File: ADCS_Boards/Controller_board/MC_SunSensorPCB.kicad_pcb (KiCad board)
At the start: 4 copper layers, 90.2 x 95.9 mm, 5 parts, among them J1 PC104_Connector

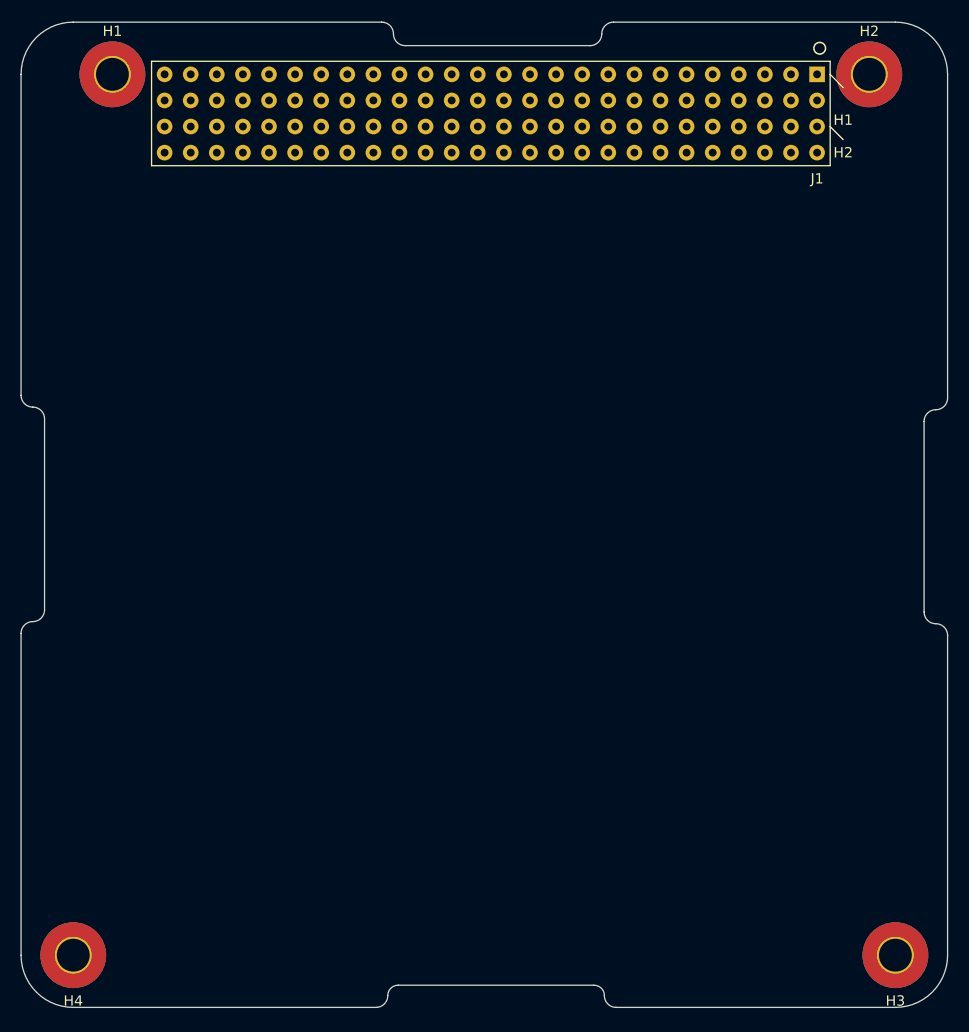
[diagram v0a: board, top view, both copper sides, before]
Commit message: adcs: Updated ADCS Controller board with latest status from Yasin
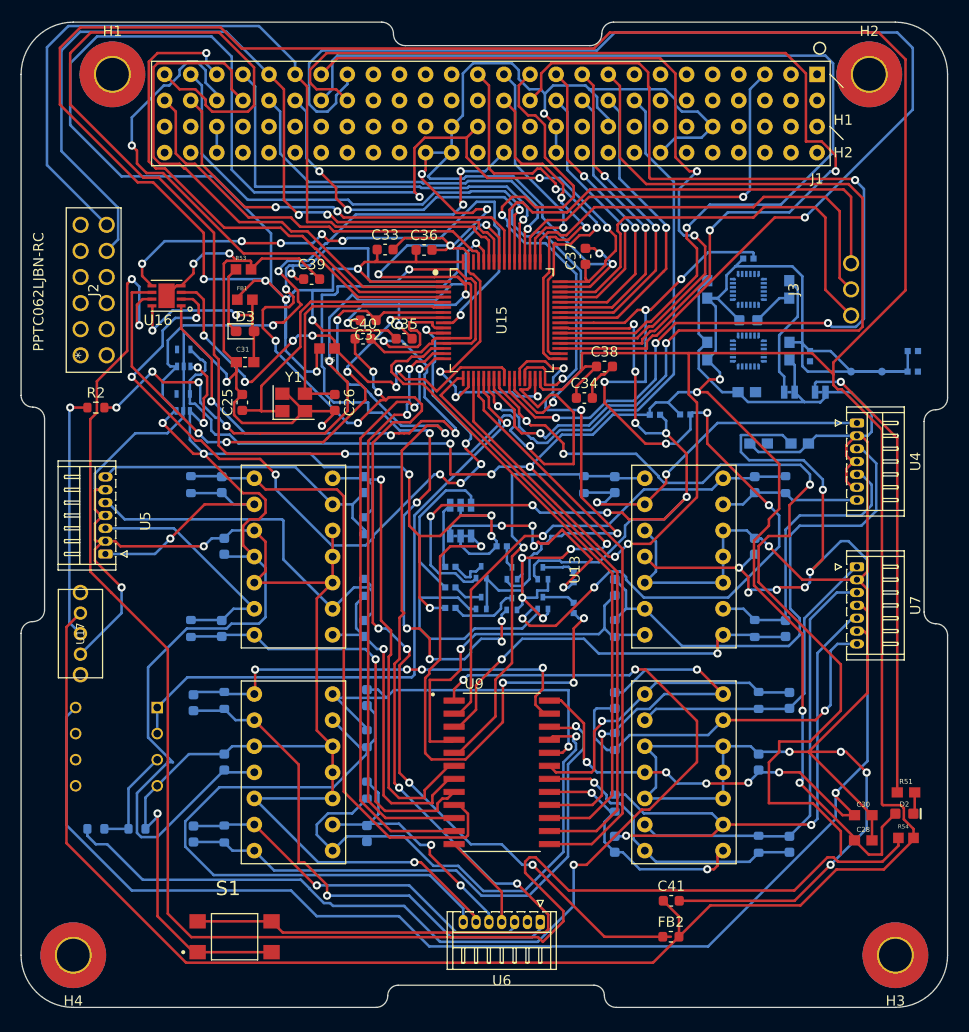
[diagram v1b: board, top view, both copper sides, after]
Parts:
- added C1: 1.0uF, SparkFun_IMU_Breakout_ICM-20948:0603, B.Cu at (184.0, 79.0)
- added C10: C, Capacitor_SMD:C_0603_1608Metric, B.Cu at (184.0, 113.0)
- added C11: C, Capacitor_SMD:C_0603_1608Metric, B.Cu at (184.0, 127.0)
- added C12: C, Capacitor_SMD:C_0603_1608Metric, B.Cu at (126.0, 113.2)
- added C13: C, Capacitor_SMD:C_0603_1608Metric, B.Cu at (126.0, 126.0)
- added C14: C, Capacitor_SMD:C_0603_1608Metric, B.Cu at (167.0, 92.0)
- added C15: C, Capacitor_SMD:C_0603_1608Metric, B.Cu at (167.0, 102.0)
- added C16: C, Capacitor_SMD:C_0603_1608Metric, B.Cu at (167.0, 127.0)
- added C17: C, Capacitor_SMD:C_0603_1608Metric, B.Cu at (167.0, 113.0)
- added C18: C, Capacitor_SMD:C_0603_1608Metric, B.Cu at (142.9, 126.0)
- added C19: C, Capacitor_SMD:C_0603_1608Metric, B.Cu at (142.9, 112.7)
- added C2: C, Capacitor_SMD:C_0603_1608Metric, B.Cu at (129.0, 119.0)
- added C20: C, Capacitor_SMD:C_0603_1608Metric, B.Cu at (183.6, 106.0)
- added C21: C, Capacitor_SMD:C_0603_1608Metric, B.Cu at (180.6, 92.0)
- added C22: 0.1uF, SparkFun_IMU_Breakout_ICM-20948:0603, B.Cu at (176.0, 79.0)
- added C23: 0.1uF, SparkFun_IMU_Breakout_ICM-20948:0603, B.Cu at (179.8, 83.0)
- added C24: 1.0uF, SparkFun_IMU_Breakout_ICM-20948:0603, B.Cu at (185.0, 88.0)
- added C25: 10p, Capacitor_SMD:C_0603_1608Metric, F.Cu at (130.8, 84.0)
- added C26: 10p, Capacitor_SMD:C_0603_1608Metric, F.Cu at (139.8, 84.0)
- added C27: 1.0uF, SparkFun_IMU_Breakout_ICM-20948:0603, B.Cu at (176.0, 73.0)
- added C28: 0.1uF, SparkFun_IMU_Breakout_ICM-20948:0603, F.Cu at (191.2, 126.6)
- added C29: 0.1uF, SparkFun_IMU_Breakout_ICM-20948:0603, B.Cu at (181.0, 88.0)
- added C3: C, Capacitor_SMD:C_0603_1608Metric, B.Cu at (128.8, 92.0)
- added C30: 1.0uF, SparkFun_IMU_Breakout_ICM-20948:0603, F.Cu at (191.2, 124.2)
- added C31: 100n, STM32_Breakout:CAPC1608X90, F.Cu at (131.0, 80.1)
- added C32: 100n, Capacitor_SMD:C_0603_1608Metric, F.Cu at (143.0, 76.0)
- added C33: 10u, Capacitor_SMD:C_0603_1608Metric, F.Cu at (144.7, 69.1)
- added C34: 100n, Capacitor_SMD:C_0603_1608Metric, F.Cu at (164.0, 83.6)
- added C35: 100n, Capacitor_SMD:C_0603_1608Metric, F.Cu at (146.5, 77.8)
- added C36: 100n, Capacitor_SMD:C_0603_1608Metric, F.Cu at (148.4, 69.2)
- added C37: 100n, Capacitor_SMD:C_0603_1608Metric, F.Cu at (164.2, 69.8)
- added C38: 100n, Capacitor_SMD:C_0603_1608Metric, F.Cu at (166.0, 80.5)
- added C39: 10n, Capacitor_SMD:C_0603_1608Metric, F.Cu at (137.5, 72.0)
- added C4: C, Capacitor_SMD:C_0603_1608Metric, B.Cu at (128.8, 106.0)
- added C40: 1u, Capacitor_SMD:C_0603_1608Metric, F.Cu at (142.5, 77.8)
- added C41: 1u, Capacitor_SMD:C_0603_1608Metric, F.Cu at (172.5, 132.5)
- added C5: C, Capacitor_SMD:C_0603_1608Metric, B.Cu at (142.6, 106.0)
- added C6: C, Capacitor_SMD:C_0603_1608Metric, B.Cu at (142.6, 92.0)
- added C7: C, Capacitor_SMD:C_0603_1608Metric, B.Cu at (129.0, 98.0)
- added C8: C, Capacitor_SMD:C_0603_1608Metric, B.Cu at (180.6, 98.0)
- added C9: C, Capacitor_SMD:C_0603_1608Metric, B.Cu at (181.0, 119.0)
- added D1: RED, SparkFun_IMU_Breakout_ICM-20948:LED-0603, B.Cu at (180.0, 76.0)
- added D2: RED, SparkFun_IMU_Breakout_ICM-20948:LED-0603, F.Cu at (195.2, 124.0)
- added D3: RED, LED_SMD:LED_0603_1608Metric_Pad1.05x0.95mm_HandSolder, F.Cu at (131.0, 77.1)
- added FB1: 100R @ 100 MHz, STM32_Breakout:INDUC1607X60N, F.Cu at (131.0, 74.0)
- added FB2: FerriteBead, Inductor_SMD:L_0603_1608Metric, F.Cu at (172.5, 136.0)
- added J2: PPTC062LJBN-RC, Footprints_QSAT:PPTC062LJBN-RC, F.Cu at (115.0, 79.4)
- added J3: Conn_01x03_Female, Footprints_QSAT:1x3_Connector_Female, F.Cu at (184.9, 73.0)
- added JP2: I2C PU, SparkFun_IMU_Breakout_ICM-20948:SMT-JUMPER_3_2-NC_TRACE_SILK, B.Cu at (152.0, 94.0)
- added JP3: LED, SparkFun_IMU_Breakout_ICM-20948:SMT-JUMPER_2_NC_TRACE_SILK, B.Cu at (184.0, 83.0)
- added JP5: I2C PU, SparkFun_IMU_Breakout_ICM-20948:SMT-JUMPER_3_2-NC_TRACE_SILK, B.Cu at (152.0, 97.0)
- added JP6: LED, SparkFun_IMU_Breakout_ICM-20948:SMT-JUMPER_2_NC_TRACE_SILK, B.Cu at (187.0, 83.0)
- added Q12: 20V/0.2A/8MHz/1.2Ω/1Vth, SparkFun_IMU_Breakout_ICM-20948:SOT-416FL, B.Cu at (160.0, 100.1)
- added Q14: 20V/0.2A/8MHz/1.2Ω/1Vth, SparkFun_IMU_Breakout_ICM-20948:SOT-416FL, B.Cu at (157.0, 103.1)
- added Q3: 20V/0.2A/8MHz/1.2Ω/1Vth, SparkFun_IMU_Breakout_ICM-20948:SOT-416FL, B.Cu at (154.0, 103.0)
- added Q4: 20V/0.2A/8MHz/1.2Ω/1Vth, SparkFun_IMU_Breakout_ICM-20948:SOT-416FL, B.Cu at (154.0, 100.0)
- added Q6: 20V/0.2A/8MHz/1.2Ω/1Vth, SparkFun_IMU_Breakout_ICM-20948:SOT-416FL, B.Cu at (157.0, 100.1)
- added Q9: 20V/0.2A/8MHz/1.2Ω/1Vth, SparkFun_IMU_Breakout_ICM-20948:SOT-416FL, B.Cu at (160.0, 103.0)
- added R1: 2.2k, SparkFun_IMU_Breakout_ICM-20948:0402-TIGHT, B.Cu at (180.0, 70.0)
- added R10: R, Resistor_SMD:R_0603_1608Metric, B.Cu at (125.8, 106.0)
- added R11: R, Resistor_SMD:R_0603_1608Metric, B.Cu at (142.6, 102.0)
- added R12: R, Resistor_SMD:R_0603_1608Metric, B.Cu at (142.6, 96.0)
- added R13: R, Resistor_SMD:R_0603_1608Metric, B.Cu at (181.0, 113.0)
- added R14: R, Resistor_SMD:R_0603_1608Metric, B.Cu at (181.0, 127.0)
- added R15: R, Resistor_SMD:R_0603_1608Metric, B.Cu at (129.0, 113.0)
- added R16: R, Resistor_SMD:R_0603_1608Metric, B.Cu at (129.0, 126.0)
- added R17: R, Resistor_SMD:R_0603_1608Metric, B.Cu at (164.0, 92.0)
- added R18: R, Resistor_SMD:R_0603_1608Metric, B.Cu at (167.0, 106.0)
- added R19: R, Resistor_SMD:R_0603_1608Metric, B.Cu at (167.0, 123.0)
- added R2: 10k, Resistor_SMD:R_0603_1608Metric, F.Cu at (116.5, 84.5)
- added R20: R, Resistor_SMD:R_0603_1608Metric, B.Cu at (167.0, 117.0)
- added R21: R, Resistor_SMD:R_0603_1608Metric, B.Cu at (142.9, 121.7)
- added R22: R, Resistor_SMD:R_0603_1608Metric, B.Cu at (142.9, 116.7)
- added R23: R, Resistor_SMD:R_0603_1608Metric, B.Cu at (180.6, 106.0)
- added R24: R, Resistor_SMD:R_0603_1608Metric, B.Cu at (183.6, 92.0)
- added R26: 2.2k, SparkFun_IMU_Breakout_ICM-20948:0402-TIGHT, B.Cu at (173.9, 85.2)
- added R27: 2.2k, SparkFun_IMU_Breakout_ICM-20948:0402-TIGHT, B.Cu at (151.0, 102.0)
- added R28: 2.2k, SparkFun_IMU_Breakout_ICM-20948:0402-TIGHT, B.Cu at (196.0, 81.0)
- added R29: 2.2k, SparkFun_IMU_Breakout_ICM-20948:0402-TIGHT, B.Cu at (151.0, 100.0)
- added R3: 2.2k, SparkFun_IMU_Breakout_ICM-20948:0402-TIGHT, B.Cu at (163.0, 104.0)
- added R32: 2.2k, SparkFun_IMU_Breakout_ICM-20948:0402-TIGHT, B.Cu at (196.0, 79.0)
- added R33: 2.2k, SparkFun_IMU_Breakout_ICM-20948:0402-TIGHT, B.Cu at (156.0, 98.0)
- added R36: 220, SparkFun_IMU_Breakout_ICM-20948:0603, B.Cu at (184.0, 73.0)
- added R40: 2.2k, SparkFun_IMU_Breakout_ICM-20948:0402-TIGHT, B.Cu at (170.9, 85.2)
- added R43: 2.2k, SparkFun_IMU_Breakout_ICM-20948:0402-TIGHT, B.Cu at (163.0, 101.0)
- added R46: 2.2k, SparkFun_IMU_Breakout_ICM-20948:0402-TIGHT, B.Cu at (186.0, 79.5)
- added R47: 2.2k, SparkFun_IMU_Breakout_ICM-20948:0402-TIGHT, B.Cu at (151.0, 104.0)
- added R51: 220, SparkFun_IMU_Breakout_ICM-20948:0603, F.Cu at (195.3, 122.0)
- added R53: 2k2, STM32_Breakout:RESC1607X60N, F.Cu at (130.9, 71.0)
- added R54: 10k, STM32_Breakout:RESC1607X60N, F.Cu at (195.3, 126.4)
- added R55: 10k, STM32_Breakout:RESC1607X60N, F.Cu at (139.0, 78.8)
- added R7: 1Meg, Resistor_SMD:R_0603_1608Metric, B.Cu at (116.5, 125.5)
- added R8: 2Meg, Resistor_SMD:R_0603_1608Metric, B.Cu at (120.5, 125.5)
- added R9: R, Resistor_SMD:R_0603_1608Metric, B.Cu at (125.8, 92.0)
- added S1: TL3305CF260QG, Footprints_QSAT:SW_TL3305CF260QG, F.Cu at (130.0, 136.0)
- added TP1: 1.8V, SparkFun_IMU_Breakout_ICM-20948:PAD.03X.03, B.Cu at (193.0, 81.0)
- added TP2: 1.8V, SparkFun_IMU_Breakout_ICM-20948:PAD.03X.03, B.Cu at (190.0, 81.0)
- added U1: 9DoF IMU, SparkFun_IMU_Breakout_ICM-20948:QFN24-3X3, B.Cu at (180.0, 73.0)
- added U10: Op-Amp, Footprints_QSAT:Op-Amp, B.Cu at (129.4, 100.3)
- added U11: Op-Amp, Footprints_QSAT:Op-Amp, B.Cu at (167.4, 121.3)
- added U12: Op-Amp, Footprints_QSAT:Op-Amp, B.Cu at (129.4, 121.3)
- added U13: Op-Amp, Footprints_QSAT:Op-Amp, B.Cu at (167.4, 100.3)
- added U14: 1.8V/100mA, SparkFun_IMU_Breakout_ICM-20948:SC70, B.Cu at (125.0, 84.0)
- added U15: STM32F103RET6, Footprints_QSAT:QFP50P1200X1200X160-64N, F.Cu at (156.0, 76.0)
- added U16: MR25H10MDF, STM32_Breakout:SON65P300X300X95-8N, F.Cu at (123.4, 73.6)
- added U17: 1825232-1, Footprints_QSAT:1825232-1, F.Cu at (115.0, 106.5)
- added U2: 1.8V/100mA, SparkFun_IMU_Breakout_ICM-20948:SC70, B.Cu at (125.0, 79.7)
- added U3: 9DoF IMU, SparkFun_IMU_Breakout_ICM-20948:QFN24-3X3, B.Cu at (180.0, 79.0)
- added U4: DF13-7P-1.25DS(20), Connector_Hirose:Hirose_DF13-07P-1.25DS_1x07_P1.25mm_Horizontal, F.Cu at (190.6, 86.0)
- added U5: DF13-7P-1.25DS(20), Connector_Hirose:Hirose_DF13-07P-1.25DS_1x07_P1.25mm_Horizontal, F.Cu at (117.4, 98.8)
- added U6: DF13-7P-1.25DS(20), Connector_Hirose:Hirose_DF13-07P-1.25DS_1x07_P1.25mm_Horizontal, F.Cu at (159.8, 134.6)
- added U7: DF13-7P-1.25DS(20), Connector_Hirose:Hirose_DF13-07P-1.25DS_1x07_P1.25mm_Horizontal, F.Cu at (190.6, 100.0)
- added U8: LM358, Footprints_QSAT:DIP794W45P254L959H508Q8, B.Cu at (118.5, 117.5)
- added U9: CD74HC4067M96, Footprints_QSAT:SOIC127P1030X265-24N, F.Cu at (156.0, 120.0)
- added Y1: Crystal_GND24, Crystal:Crystal_SMD_3225-4Pin_3.2x2.5mm, F.Cu at (135.8, 84.0)
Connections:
- J1 pad 100: unconnected-(J1-Pad100) -> GND
- J1 pad 16: unconnected-(J1-Pad16) -> PA6
- J1 pad 17: unconnected-(J1-Pad17) -> PA7
- J1 pad 18: unconnected-(J1-Pad18) -> PA8
- J1 pad 19: unconnected-(J1-Pad19) -> PA9
- J1 pad 20: unconnected-(J1-Pad20) -> PA10
- J1 pad 21: unconnected-(J1-Pad21) -> PA11
- J1 pad 22: unconnected-(J1-Pad22) -> PA12
- J1 pad 23: unconnected-(J1-Pad23) -> PB10
- J1 pad 24: unconnected-(J1-Pad24) -> PB0
- J1 pad 25: unconnected-(J1-Pad25) -> PA15
- J1 pad 26: unconnected-(J1-Pad26) -> PB12
- J1 pad 27: unconnected-(J1-Pad27) -> PB13
- J1 pad 37: unconnected-(J1-Pad37) -> PB14
- J1 pad 38: unconnected-(J1-Pad38) -> PB15
- J1 pad 39: unconnected-(J1-Pad39) -> PC6
- J1 pad 40: unconnected-(J1-Pad40) -> PC7
- J1 pad 41: unconnected-(J1-Pad41) -> Net-(J1-Pad41)
- J1 pad 42: unconnected-(J1-Pad42) -> PB1
- J1 pad 43: unconnected-(J1-Pad43) -> Net-(J1-Pad43)
- J1 pad 44: unconnected-(J1-Pad44) -> PC11
- J1 pad 45: unconnected-(J1-Pad45) -> PC12
- J1 pad 46: unconnected-(J1-Pad46) -> PC13
- J1 pad 47: unconnected-(J1-Pad47) -> PC14
- J1 pad 48: unconnected-(J1-Pad48) -> PC15
- J1 pad 49: unconnected-(J1-Pad49) -> PD2
- J1 pad 5: unconnected-(J1-Pad5) -> PC10
- J1 pad 50: unconnected-(J1-Pad50) -> PB4
- J1 pad 51: unconnected-(J1-Pad51) -> PB11
- J1 pad 52: unconnected-(J1-Pad52) -> PB8
- J1 pad 61: unconnected-(J1-Pad61) -> GND
- J1 pad 66: unconnected-(J1-Pad66) -> GND
- J1 pad 69: unconnected-(J1-Pad69) -> GND
- J1 pad 73: unconnected-(J1-Pad73) -> GND
- J1 pad 74: unconnected-(J1-Pad74) -> GND
- J1 pad 78: unconnected-(J1-Pad78) -> +5V
- J1 pad 79: unconnected-(J1-Pad79) -> +3V3
- J1 pad 81: unconnected-(J1-Pad81) -> GND
- J1 pad 82: unconnected-(J1-Pad82) -> GND
- J1 pad 84: unconnected-(J1-Pad84) -> GND
- J1 pad 99: unconnected-(J1-Pad99) -> GND
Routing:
- net GND: track 0.00 -> 668.1 mm, vias 0 -> 26
- net +3V3: track 0.00 -> 603.4 mm, vias 0 -> 11
- net +5V: track 0.00 -> 423.0 mm, vias 0 -> 24
- net GPIO1: track 0.00 -> 254.8 mm, vias 0 -> 5
- net 1.8V: track 0.00 -> 232.9 mm, vias 0 -> 12
- net +3.3VA: track 0.00 -> 145.8 mm, vias 0 -> 11
- net PB11: track 0.00 -> 133.7 mm, vias 0 -> 2
- net /NRST: track 0.00 -> 124.4 mm, vias 0 -> 4
- net PB14: track 0.00 -> 121.5 mm, vias 0 -> 1
- net IMU_SDA: track 0.00 -> 119.9 mm, vias 0 -> 8
- net MuxOut_1: track 0.00 -> 105.5 mm, vias 0 -> 3
- net PB15: track 0.00 -> 103.6 mm, vias 0 -> 2
- net PB0: track 0.00 -> 101.8 mm, vias 0 -> 4
- net PC7: track 0.00 -> 100.3 mm, vias 0 -> 1
- net PA7: track 0.00 -> 92.5 mm, vias 0 -> 2
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- added copper zone on In2.Cu, net +5V
- added copper zone on In1.Cu, net GND
